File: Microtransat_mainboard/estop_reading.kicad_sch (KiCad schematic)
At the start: 4 parts, among them J301 ESTOP IN, K301 12V SRD Form C

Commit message: update resistor
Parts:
- R301: footprint Resistor_THT:R_Axial_DIN0207_L6.3mm_D2.5mm_P10.16mm_Horizontal -> Resistor_SMD:R_1206_3216Metric_Pad1.30x1.75mm_HandSolder
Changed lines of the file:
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@@
 			)
 		)
-		(property "Footprint" "Resistor_THT:R_Axial_DIN0207_L6.3mm_D2.5mm_P10.16mm_Horizontal"
+		(property "Footprint" "Resistor_SMD:R_1206_3216Metric_Pad1.30x1.75mm_HandSolder"
 			(at 143.256 110.744 90)
 			(effects

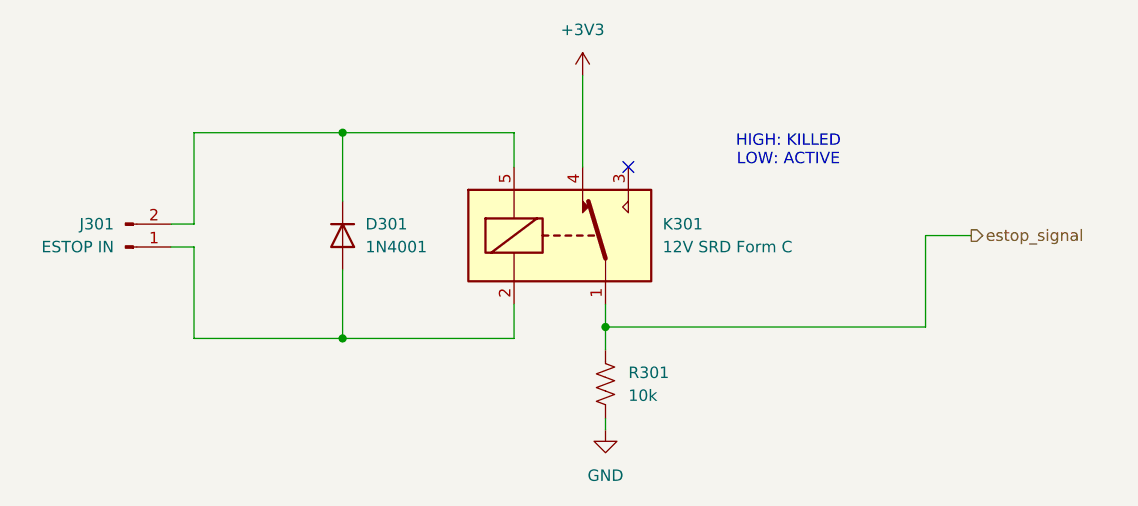
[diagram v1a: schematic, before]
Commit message: Finished silkscreen/outline changes
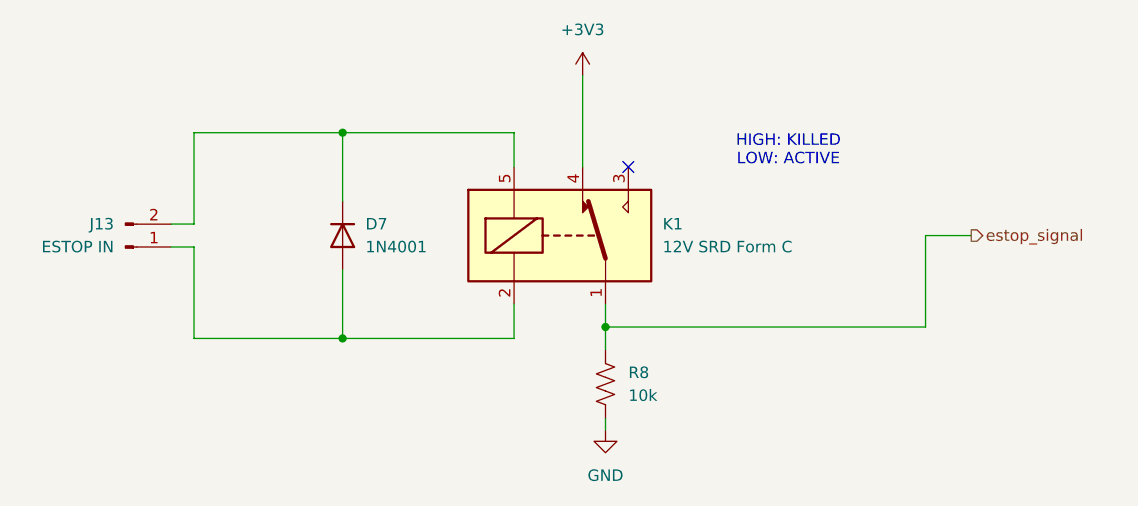
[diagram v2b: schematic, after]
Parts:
- renumbered D301 to D7, J301 to J13, K301 to K1, R301 to R8
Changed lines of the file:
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@@
 		(dnp no)
 		(fields_autoplaced yes)
-		(property "Reference" "R301"
+		(property "Reference" "R8"
 			(at 144.78 109.2199 0)
 			(effects
@@
 			(project "Microtransat_mainboard"
 				(path "/89914625-be83-416e-bb0d-b792f59b4aa6/82ad2dad-7ed6-420b-b0db-54c534917ded"
-					(reference "R301")
+					(reference "R8")
 					(unit 1)
 				)
@@
 		(dnp no)
 		(fields_autoplaced yes)
-		(property "Reference" "#PWR0302"
+		(property "Reference" "#PWR044"
 			(at 142.24 121.92 0)
 			(effects
@@
 			(project "Microtransat_mainboard"
 				(path "/89914625-be83-416e-bb0d-b792f59b4aa6/82ad2dad-7ed6-420b-b0db-54c534917ded"
-					(reference "#PWR0302")
+					(reference "#PWR044")
 					(unit 1)
 				)
@@
 		(dnp no)
 		(fields_autoplaced yes)
-		(property "Reference" "D301"
+		(property "Reference" "D7"
 			(at 115.57 92.7099 90)
 			(effects
@@
 			(project "Microtransat_mainboard"
 				(path "/89914625-be83-416e-bb0d-b792f59b4aa6/82ad2dad-7ed6-420b-b0db-54c534917ded"
-					(reference "D301")
+					(reference "D7")
 					(unit 1)
 				)
@@
 		(dnp no)
 		(fields_autoplaced yes)
-		(property "Reference" "J301"
+		(property "Reference" "J13"
 			(at 87.63 92.7099 0)
 			(effects
@@
 			(project "Microtransat_mainboard"
 				(path "/89914625-be83-416e-bb0d-b792f59b4aa6/82ad2dad-7ed6-420b-b0db-54c534917ded"
-					(reference "J301")
+					(reference "J13")
 					(unit 1)
 				)
@@
 		(dnp no)
 		(fields_autoplaced yes)
-		(property "Reference" "K301"
+		(property "Reference" "K1"
 			(at 148.59 92.7099 0)
 			(effects
@@
 			(project "Microtransat_mainboard"
 				(path "/89914625-be83-416e-bb0d-b792f59b4aa6/82ad2dad-7ed6-420b-b0db-54c534917ded"
-					(reference "K301")
+					(reference "K1")
 					(unit 1)
 				)
@@
 		(dnp no)
 		(fields_autoplaced yes)
-		(property "Reference" "#PWR0301"
+		(property "Reference" "#PWR043"
 			(at 139.7 80.01 0)
 			(effects
@@
 			(project "Microtransat_mainboard"
 				(path "/89914625-be83-416e-bb0d-b792f59b4aa6/82ad2dad-7ed6-420b-b0db-54c534917ded"
-					(reference "#PWR0301")
-					(unit 1)
-				)
+					(reference "#PWR043")
+					(unit 1)
+				)

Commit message: Some small changes to silkscreen and component numbers
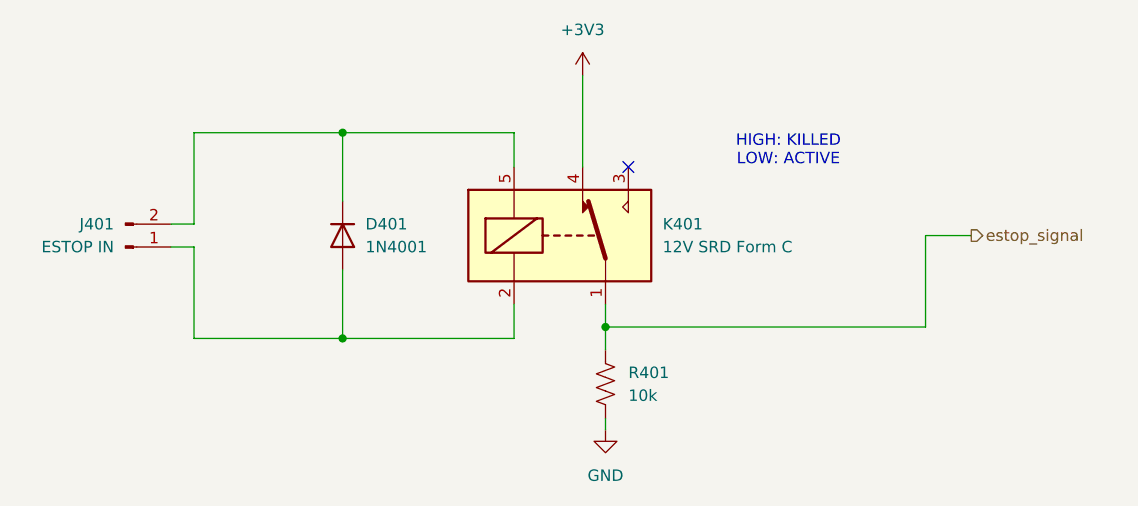
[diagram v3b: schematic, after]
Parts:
- renumbered D7 to D401, J13 to J401, K1 to K401, R8 to R401
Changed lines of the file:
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@@
 		(dnp no)
 		(fields_autoplaced yes)
-		(property "Reference" "R8"
+		(property "Reference" "R401"
 			(at 144.78 109.2199 0)
 			(effects
@@
 			(project "Microtransat_mainboard"
 				(path "/89914625-be83-416e-bb0d-b792f59b4aa6/82ad2dad-7ed6-420b-b0db-54c534917ded"
-					(reference "R8")
+					(reference "R401")
 					(unit 1)
 				)
@@
 		(dnp no)
 		(fields_autoplaced yes)
-		(property "Reference" "#PWR044"
+		(property "Reference" "#PWR0402"
 			(at 142.24 121.92 0)
 			(effects
@@
 			(project "Microtransat_mainboard"
 				(path "/89914625-be83-416e-bb0d-b792f59b4aa6/82ad2dad-7ed6-420b-b0db-54c534917ded"
-					(reference "#PWR044")
+					(reference "#PWR0402")
 					(unit 1)
 				)
@@
 		(dnp no)
 		(fields_autoplaced yes)
-		(property "Reference" "D7"
+		(property "Reference" "D401"
 			(at 115.57 92.7099 90)
 			(effects
@@
 			(project "Microtransat_mainboard"
 				(path "/89914625-be83-416e-bb0d-b792f59b4aa6/82ad2dad-7ed6-420b-b0db-54c534917ded"
-					(reference "D7")
+					(reference "D401")
 					(unit 1)
 				)
@@
 		(dnp no)
 		(fields_autoplaced yes)
-		(property "Reference" "J13"
+		(property "Reference" "J401"
 			(at 87.63 92.7099 0)
 			(effects
@@
 			(project "Microtransat_mainboard"
 				(path "/89914625-be83-416e-bb0d-b792f59b4aa6/82ad2dad-7ed6-420b-b0db-54c534917ded"
-					(reference "J13")
+					(reference "J401")
 					(unit 1)
 				)
@@
 		(dnp no)
 		(fields_autoplaced yes)
-		(property "Reference" "K1"
+		(property "Reference" "K401"
 			(at 148.59 92.7099 0)
 			(effects
@@
 			(project "Microtransat_mainboard"
 				(path "/89914625-be83-416e-bb0d-b792f59b4aa6/82ad2dad-7ed6-420b-b0db-54c534917ded"
-					(reference "K1")
+					(reference "K401")
 					(unit 1)
 				)
@@
 		(dnp no)
 		(fields_autoplaced yes)
-		(property "Reference" "#PWR043"
+		(property "Reference" "#PWR0401"
 			(at 139.7 80.01 0)
 			(effects
@@
 			(project "Microtransat_mainboard"
 				(path "/89914625-be83-416e-bb0d-b792f59b4aa6/82ad2dad-7ed6-420b-b0db-54c534917ded"
-					(reference "#PWR043")
-					(unit 1)
-				)
+					(reference "#PWR0401")
+					(unit 1)
+				)
